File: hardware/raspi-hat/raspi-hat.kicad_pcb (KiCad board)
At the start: 4 copper layers, 65 x 57 mm, 55 parts, among them J1 Conn_02x05_Counter_Clockwise, J2 Conn_01x03_Pin, J3 ATX-20, J4 Raspberry_Pi_4, J5 USB3_A, Q1 FDMS86101, Q2 FDMS86101, Q3 FDMS86101, Q4 FDMS86101, Q5 FDMS86101, Q7 FDMS86101, U1 STSPIN32G4, Y1 Crystal_GND23_Small

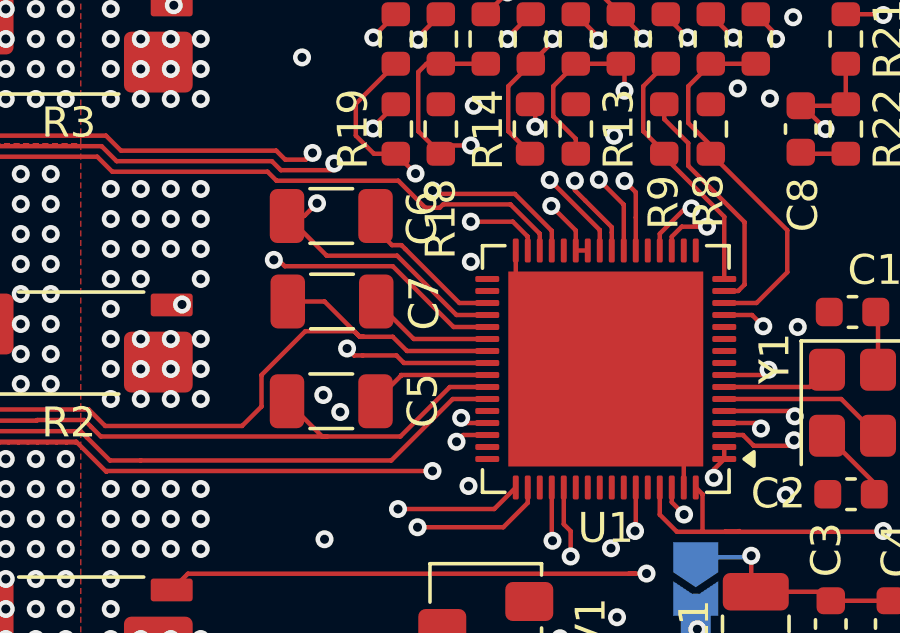
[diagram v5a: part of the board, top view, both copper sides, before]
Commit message: - some readability improvements - some routing updates
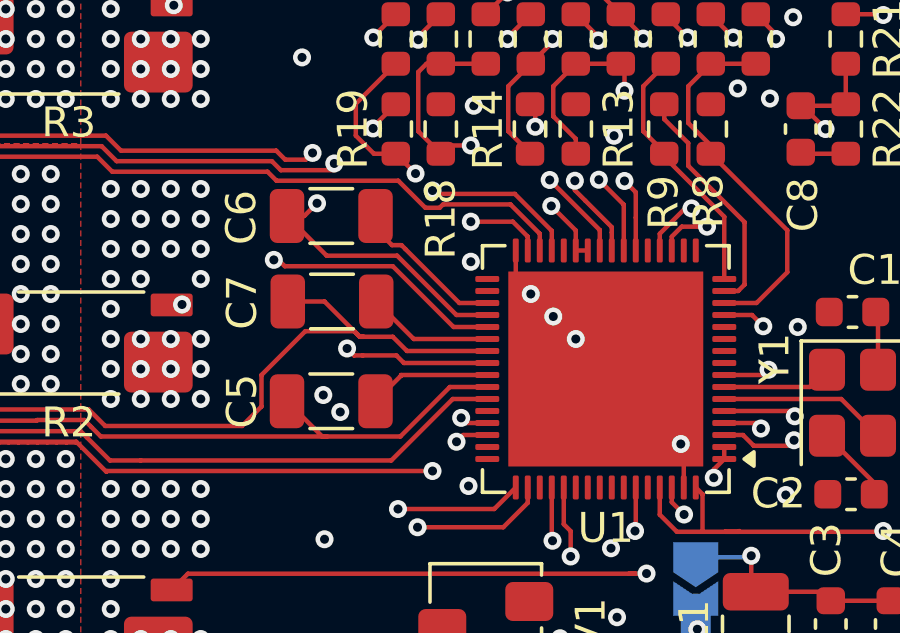
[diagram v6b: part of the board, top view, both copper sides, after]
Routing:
- net /+3V3: track 102.6 -> 98.5 mm
- net /controller/hall_2: track 79.0 -> 78.1 mm
- net /controller/hall_3: track 77.6 -> 76.7 mm
- net /controller/hall_1: track 79.7 -> 79.1 mm
- net /GND: vias 114 -> 118

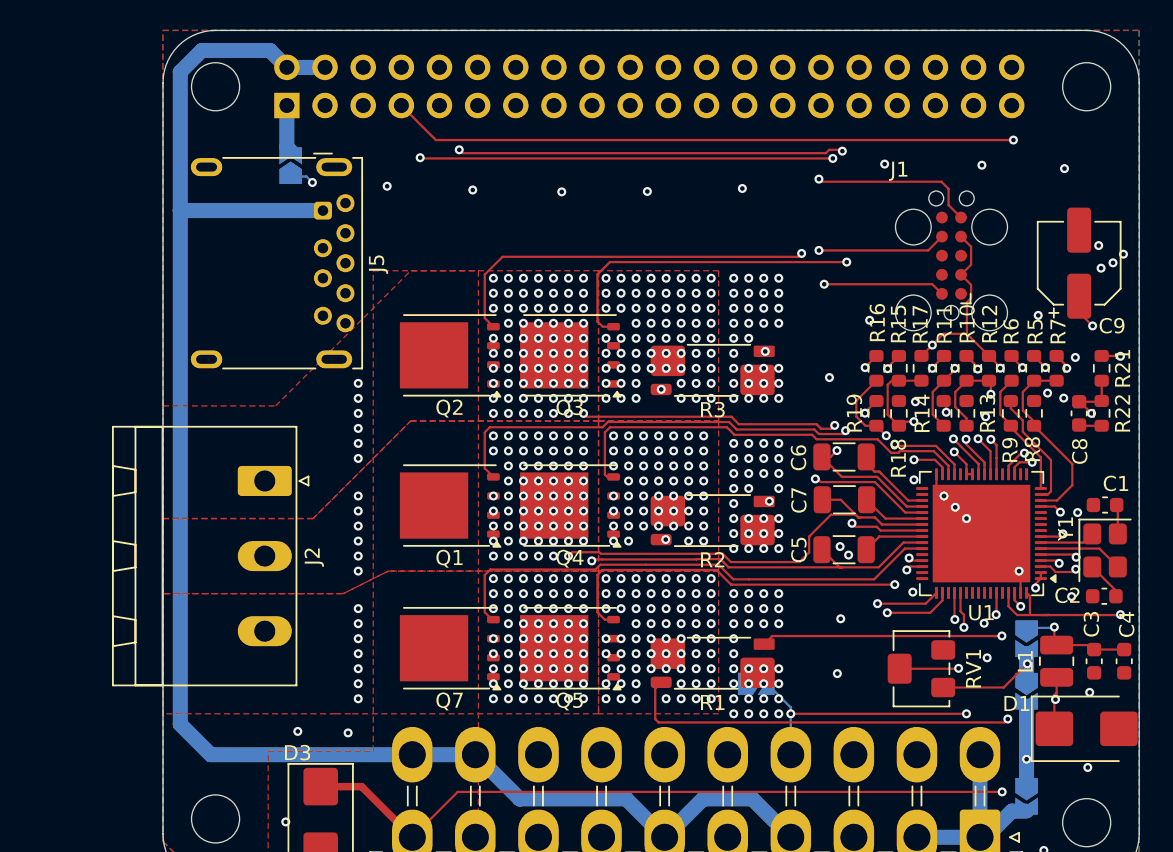
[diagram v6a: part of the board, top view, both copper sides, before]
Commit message: adapted some parts
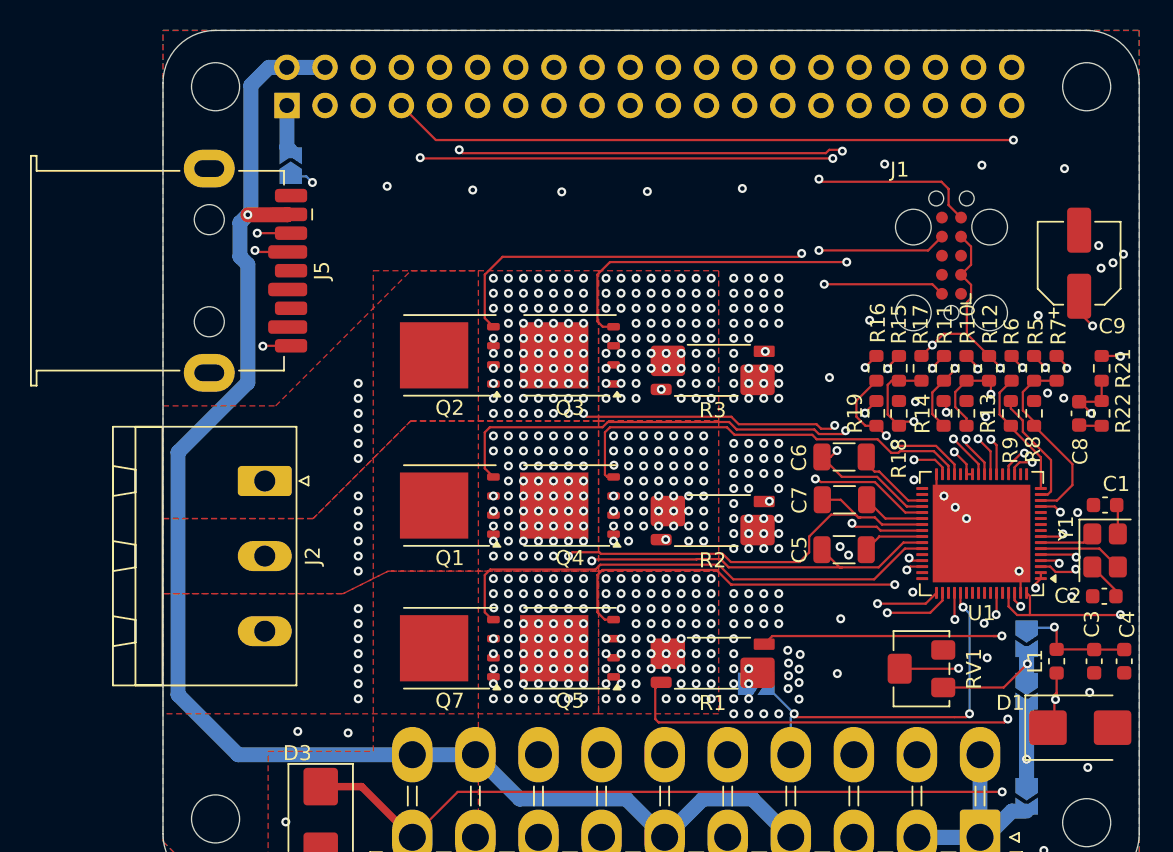
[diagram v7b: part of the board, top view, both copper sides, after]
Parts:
- J5: footprint Connector_USB:USB3_A_Molex_48393-001 -> Connector_USB:USB3_A_Receptacle_Wuerth_692122030100
- L1: footprint Inductor_SMD:L_1008_2520Metric -> Inductor_SMD:L_0603_1608Metric
- moved J5 11.7 mm to (99.6, 116.0)
- moved D1 0.43 mm to (161.1, 146.4)
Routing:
- net /+5V: track 109.5 -> 98.0 mm, vias 0 -> 1
- net /controller/shunt-amp1/OP-: track 22.2 -> 13.1 mm, vias 3 -> 2
- net /controller/hall_3: track 76.7 -> 84.9 mm, vias 2 -> 3
- net /controller/hall_1: track 79.1 -> 85.3 mm, vias 2 -> 3
- net /controller/hall_2: track 78.1 -> 83.7 mm, vias 2 -> 3
- net /controller/inverter/LS3: track 39.7 -> 39.1 mm
- net /controller/shunt2_l: track 20.2 -> 19.6 mm
- net /GND: vias 118 -> 120

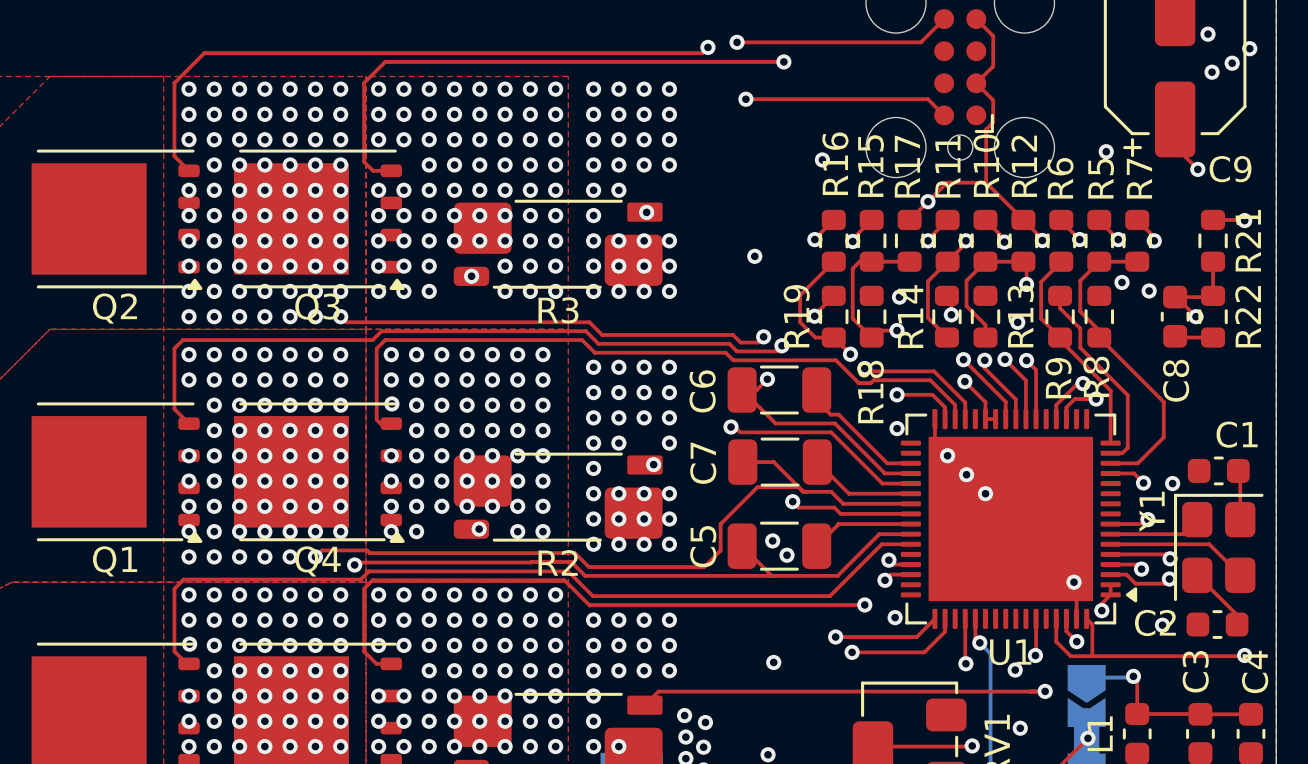
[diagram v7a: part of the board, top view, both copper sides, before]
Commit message: - added ntc for temperature sensing - documented calculation for ntc voltage output in software/docs/ntc.ipynb - added gnd planes for all layers
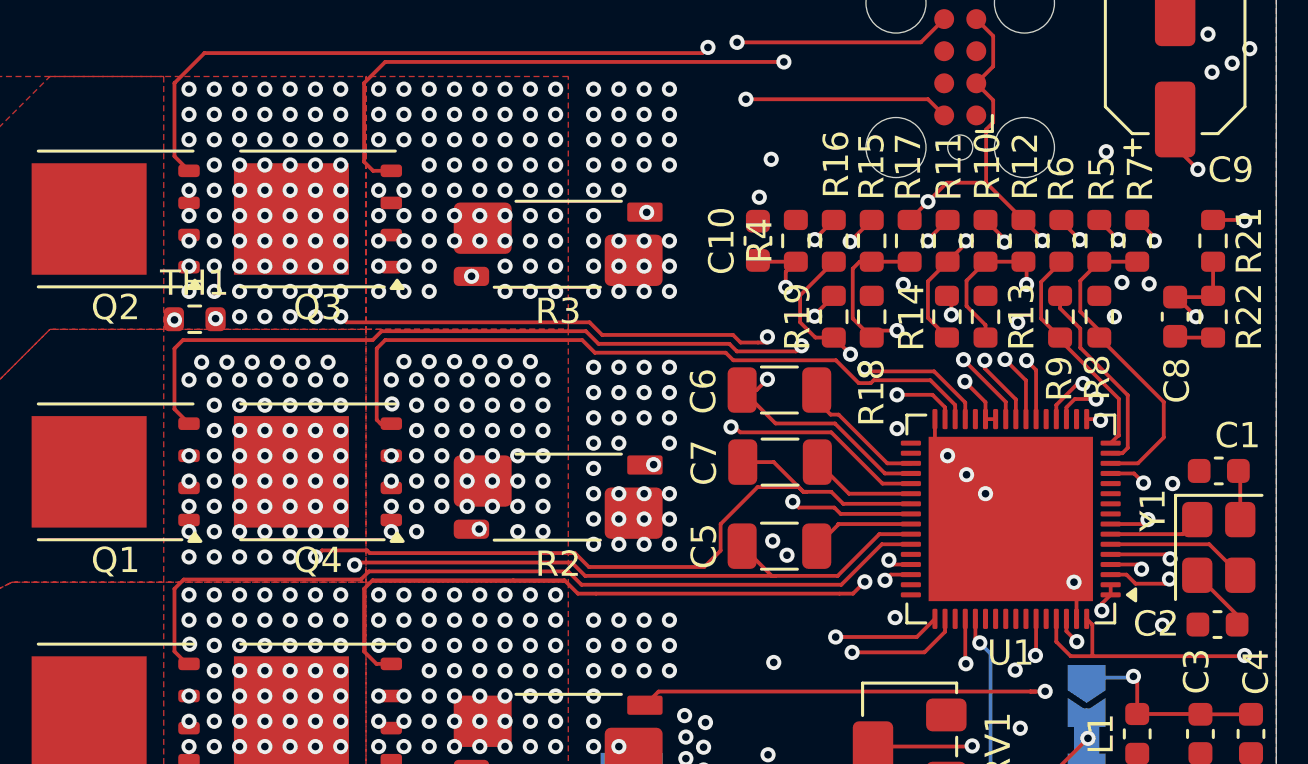
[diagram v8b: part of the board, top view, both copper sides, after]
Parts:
- added C10: 1u, Capacitor_SMD:C_0603_1608Metric, F.Cu at (144.5, 122.5)
- added R4: 10k, Resistor_SMD:R_0603_1608Metric, F.Cu at (146.0, 122.5)
- added TH1: 10k, Resistor_SMD:R_0603_1608Metric, F.Cu at (122.2, 125.6)
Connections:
- U1 pad 17: unconnected-(U1-PA4-Pad17) -> /controller/ntc
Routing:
- net /controller/ntc: track 0.00 -> 48.3 mm, vias 0 -> 4
- net /controller/v_mc: track 61.1 -> 94.9 mm, vias 6 -> 8
- net /controller/shunt-amp1/OPOUT: track 16.0 -> 12.9 mm
- net /controller/shunt2_h: track 37.6 -> 39.6 mm
- net /controller/inverter/LS1: track 38.7 -> 37.7 mm
- net /controller/inverter/HS2: track 39.3 -> 39.9 mm
- net /controller/phase_w: track 28.2 -> 28.4 mm, vias 77 -> 75
- net Net-(Q4-S-Pad1): vias 52 -> 51
- net /controller/phase_v: vias 66 -> 65
- net /GND: vias 120 -> 119
- added copper zone on In1.Cu, net /GND
- added copper zone on In2.Cu, net /GND
